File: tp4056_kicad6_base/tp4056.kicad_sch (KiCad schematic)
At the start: 33 parts, among them J1 Conn_01x01_Female, J2 Conn_01x01_Female, J3 USB_B_Micro, J4 Conn_01x02_Male, J6 Conn_01x05_Male, Q1 AO3401A, Q2 FS8205A, Q3 AO3401A, U1 TP4056, U2 DW01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

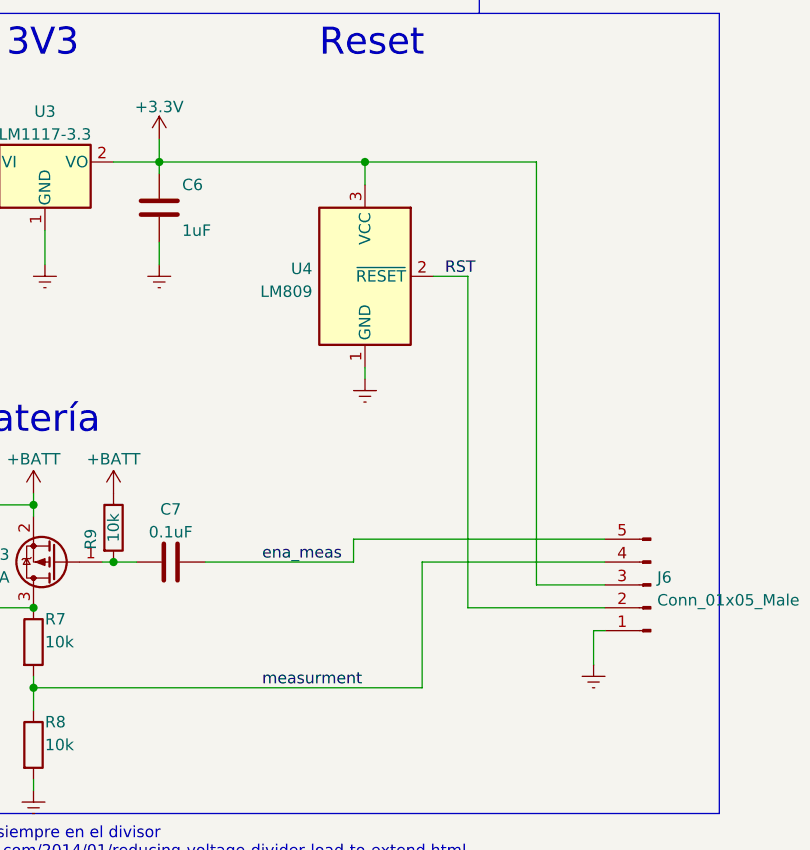
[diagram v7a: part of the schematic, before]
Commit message: PCB 40x25. To check DRC
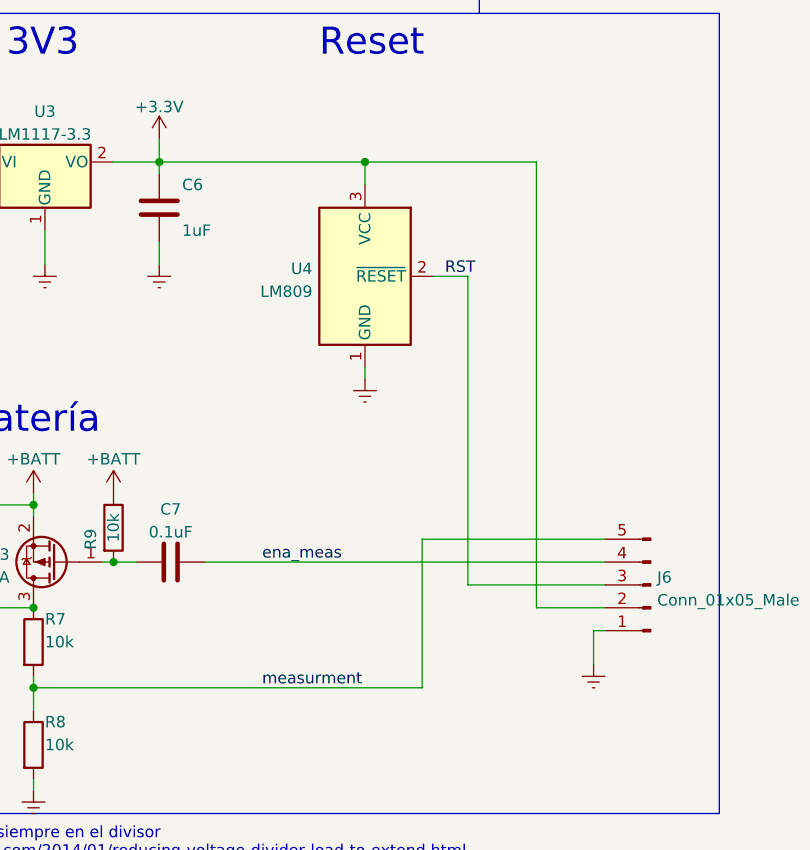
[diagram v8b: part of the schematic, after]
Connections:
- net +3.3V: now also J6.2 (Pin_2); no longer J6.3 (Pin_3)
- net RST: now also J6.3 (Pin_3); no longer J6.2 (Pin_2)
- net ena_meas: now also J6.4 (Pin_4); no longer J6.5 (Pin_5)
- net measurment: now also J6.5 (Pin_5); no longer J6.4 (Pin_4)
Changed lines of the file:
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@@
   (no_connect (at 39.37 59.69))
   (no_connect (at 86.36 104.14))
-  (wire (pts (xy 227.33 121.92) (xy 227.33 124.46))
-    (stroke (width 0) (type default) (color 0 0 0 0))
-  )
   (wire (pts (xy 185.42 80.01) (xy 179.07 80.01))
     (stroke (width 0) (type default) (color 0 0 0 0))
@@
     (stroke (width 0) (type default) (color 0 0 0 0))
   )
-  (wire (pts (xy 255.27 121.92) (xy 227.33 121.92))
-    (stroke (width 0) (type default) (color 0 0 0 0))
-  )
   (wire (pts (xy 140.97 129.54) (xy 140.97 134.62))
     (stroke (width 0) (type default) (color 0 0 0 0))
@@
     (stroke (width 0) (type default) (color 0 0 0 0))
   )
-  (wire (pts (xy 227.33 124.46) (xy 210.82 124.46))
+  (wire (pts (xy 210.82 124.46) (xy 255.27 124.46))
     (stroke (width 0) (type default) (color 0 0 0 0))
   )
@@
     (stroke (width 0) (type default) (color 0 0 0 0))
   )
-  (wire (pts (xy 247.65 80.01) (xy 247.65 127))
+  (wire (pts (xy 247.65 80.01) (xy 247.65 129.54))
     (stroke (width 0) (type default) (color 0 0 0 0))
   )
@@
     (stroke (width 0) (type default) (color 0 0 0 0))
   )
-  (wire (pts (xy 240.03 92.71) (xy 240.03 129.54))
+  (wire (pts (xy 240.03 92.71) (xy 240.03 127))
     (stroke (width 0) (type default) (color 0 0 0 0))
   )
@@
     (stroke (width 0) (type default) (color 0 0 0 0))
   )
-  (wire (pts (xy 240.03 129.54) (xy 255.27 129.54))
-    (stroke (width 0) (type default) (color 0 0 0 0))
-  )
-  (wire (pts (xy 234.95 124.46) (xy 255.27 124.46))
+  (wire (pts (xy 240.03 127) (xy 255.27 127))
+    (stroke (width 0) (type default) (color 0 0 0 0))
+  )
+  (wire (pts (xy 234.95 121.92) (xy 255.27 121.92))
     (stroke (width 0) (type default) (color 0 0 0 0))
   )
@@
     (stroke (width 0) (type default) (color 0 0 0 0))
   )
-  (wire (pts (xy 234.95 124.46) (xy 234.95 138.43))
+  (wire (pts (xy 234.95 121.92) (xy 234.95 138.43))
     (stroke (width 0) (type default) (color 0 0 0 0))
   )
@@
     (stroke (width 0) (type default) (color 0 0 0 0))
   )
-  (wire (pts (xy 247.65 127) (xy 255.27 127))
-    (stroke (width 0) (type default) (color 0 0 0 0))
-  )
+  (wire (pts (xy 247.65 129.54) (xy 255.27 129.54))
+    (stroke (width 0) (type default) (color 0 0 0 0))
+  )
